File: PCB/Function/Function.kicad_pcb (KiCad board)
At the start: 2 copper layers, 101.6 x 152.4 mm, 47 parts, among them J1 MTA156-3, J2 MTA156-3, J3 MN12, J4 MN12, J5 MN12, J6 MBNF15, J7 MBNF15, U1 AD823, U12 4013, U2 ADR5045, U3 AD823

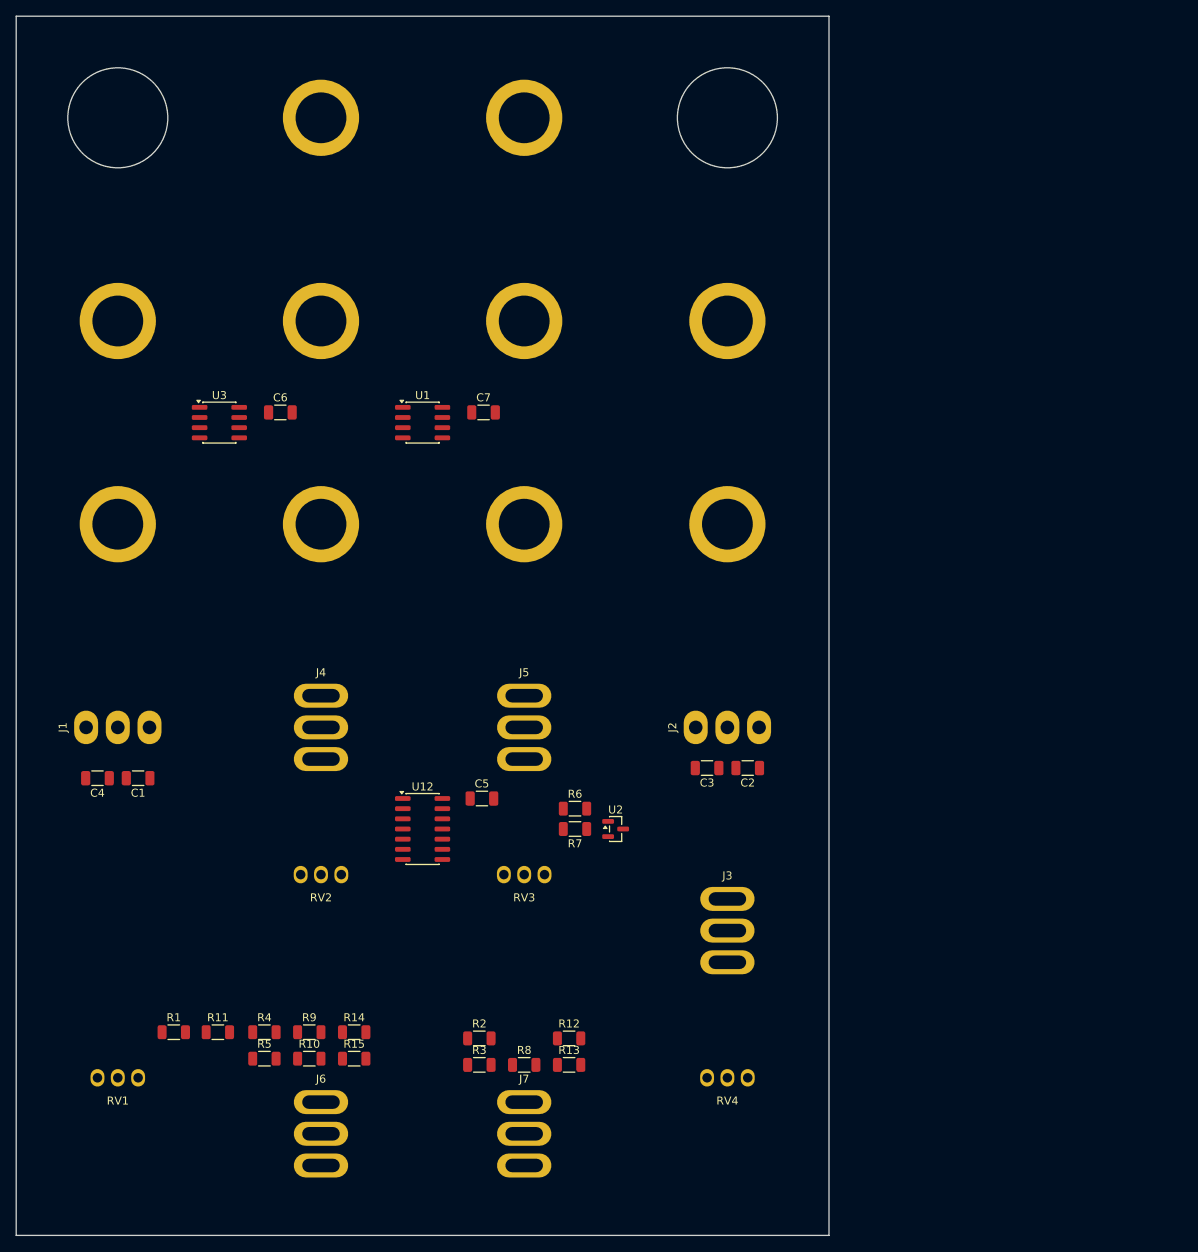
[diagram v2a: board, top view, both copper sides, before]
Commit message: Start placement
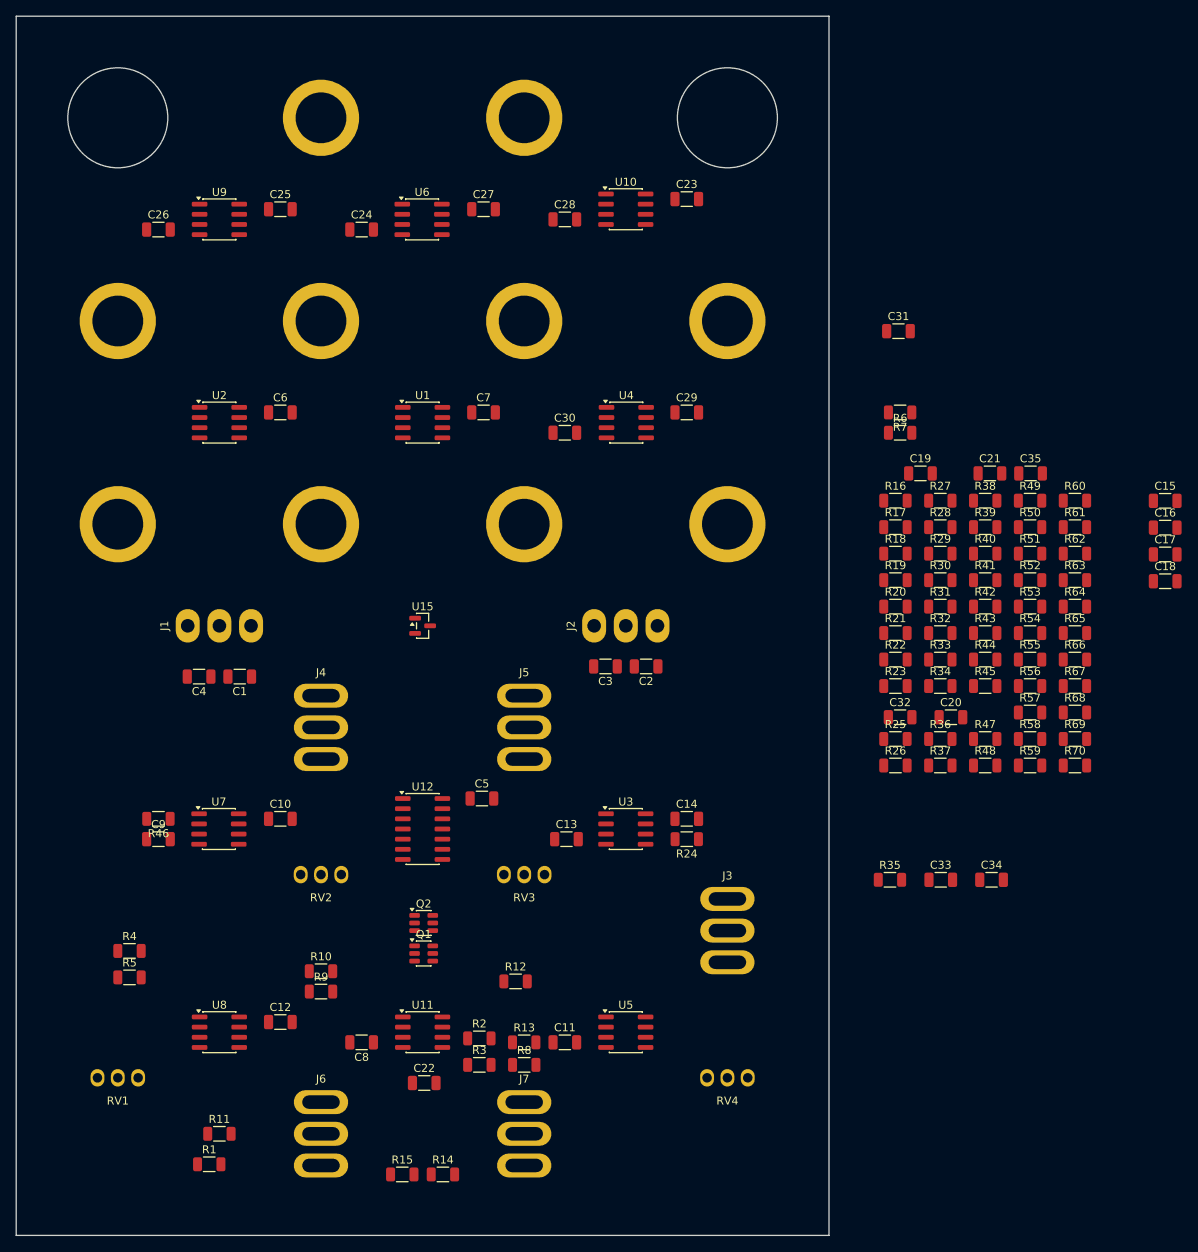
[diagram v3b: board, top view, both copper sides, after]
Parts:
- added C10: 100n, Capacitor_SMD:C_1206_3216Metric, F.Cu at (58.4, 125.7)
- added C11: 100n, Capacitor_SMD:C_1206_3216Metric, F.Cu at (94.0, 153.7)
- added C12: 100n, Capacitor_SMD:C_1206_3216Metric, F.Cu at (58.4, 151.1)
- added C13: 100n, Capacitor_SMD:C_1206_3216Metric, F.Cu at (94.2, 128.3)
- added C14: 100n, Capacitor_SMD:C_1206_3216Metric, F.Cu at (109.2, 125.7)
- added C15: 100n, Capacitor_SMD:C_1206_3216Metric, F.Cu at (169.0, 86.0)
- added C16: 100n, Capacitor_SMD:C_1206_3216Metric, F.Cu at (169.0, 89.3)
- added C17: 100n, Capacitor_SMD:C_1206_3216Metric, F.Cu at (169.0, 92.7)
- added C18: 47p, Capacitor_SMD:C_1206_3216Metric, F.Cu at (169.0, 96.0)
- added C19: 47p, Capacitor_SMD:C_1206_3216Metric, F.Cu at (138.4, 82.5)
- added C20: 47p, Capacitor_SMD:C_1206_3216Metric, F.Cu at (142.2, 113.0)
- added C21: 47p, Capacitor_SMD:C_1206_3216Metric, F.Cu at (147.1, 82.5)
- added C22: 4n7, Capacitor_SMD:C_1206_3216Metric, F.Cu at (76.4, 158.8)
- added C23: 100n, Capacitor_SMD:C_1206_3216Metric, F.Cu at (109.2, 48.3)
- added C24: 100n, Capacitor_SMD:C_1206_3216Metric, F.Cu at (68.6, 52.1)
- added C25: 100n, Capacitor_SMD:C_1206_3216Metric, F.Cu at (58.4, 49.5)
- added C26: 100n, Capacitor_SMD:C_1206_3216Metric, F.Cu at (43.2, 52.1)
- added C27: 100n, Capacitor_SMD:C_1206_3216Metric, F.Cu at (83.8, 49.5)
- added C28: 100n, Capacitor_SMD:C_1206_3216Metric, F.Cu at (94.0, 50.8)
- added C29: 100n, Capacitor_SMD:C_1206_3216Metric, F.Cu at (109.2, 74.9)
- added C30: 100n, Capacitor_SMD:C_1206_3216Metric, F.Cu at (94.0, 77.5)
- added C31: 47p, Capacitor_SMD:C_1206_3216Metric, F.Cu at (135.7, 64.8)
- added C32: 47p, Capacitor_SMD:C_1206_3216Metric, F.Cu at (135.9, 113.0)
- added C33: 47p, Capacitor_SMD:C_1206_3216Metric, F.Cu at (141.0, 133.3)
- added C34: 47p, Capacitor_SMD:C_1206_3216Metric, F.Cu at (147.3, 133.3)
- added C35: 47p, Capacitor_SMD:C_1206_3216Metric, F.Cu at (152.2, 82.5)
- added C8: 100n, Capacitor_SMD:C_1206_3216Metric, F.Cu at (68.6, 153.7)
- added C9: 100n, Capacitor_SMD:C_1206_3216Metric, F.Cu at (43.2, 128.3)
- added Q1: BC847, Package_TO_SOT_SMD:SOT-23-6, F.Cu at (76.3, 142.6)
- added Q2: BCM857, Package_TO_SOT_SMD:SOT-23-6, F.Cu at (76.3, 138.8)
- added R16: 4K7, Resistor_SMD:R_1206_3216Metric, F.Cu at (135.3, 86.0)
- added R17: 150K, Resistor_SMD:R_1206_3216Metric, F.Cu at (135.3, 89.3)
- added R18: 6M8, Resistor_SMD:R_1206_3216Metric, F.Cu at (135.3, 92.6)
- added R19: 47K, Resistor_SMD:R_1206_3216Metric, F.Cu at (135.3, 95.9)
- added R20: 470, Resistor_SMD:R_1206_3216Metric, F.Cu at (135.3, 99.2)
- added R21: 47K, Resistor_SMD:R_1206_3216Metric, F.Cu at (135.3, 102.5)
- added R22: 100K, Resistor_SMD:R_1206_3216Metric, F.Cu at (135.3, 105.8)
- added R23: 33K, Resistor_SMD:R_1206_3216Metric, F.Cu at (135.3, 109.1)
- added R24: 47K, Resistor_SMD:R_1206_3216Metric, F.Cu at (109.2, 128.3)
- added R25: 100K, Resistor_SMD:R_1206_3216Metric, F.Cu at (135.3, 115.8)
- added R26: 33K, Resistor_SMD:R_1206_3216Metric, F.Cu at (135.3, 119.1)
- added R27: 47K, Resistor_SMD:R_1206_3216Metric, F.Cu at (140.9, 86.0)
- added R28: 470, Resistor_SMD:R_1206_3216Metric, F.Cu at (140.9, 89.3)
- added R29: 47K, Resistor_SMD:R_1206_3216Metric, F.Cu at (140.9, 92.6)
- added R30: 47K, Resistor_SMD:R_1206_3216Metric, F.Cu at (140.9, 95.9)
- added R31: 47K, Resistor_SMD:R_1206_3216Metric, F.Cu at (140.9, 99.2)
- added R32: 47K, Resistor_SMD:R_1206_3216Metric, F.Cu at (140.9, 102.5)
- added R33: 470, Resistor_SMD:R_1206_3216Metric, F.Cu at (140.9, 105.8)
- added R34: 47K, Resistor_SMD:R_1206_3216Metric, F.Cu at (140.9, 109.1)
- added R35: 47K, Resistor_SMD:R_1206_3216Metric, F.Cu at (134.6, 133.3)
- added R36: 47K, Resistor_SMD:R_1206_3216Metric, F.Cu at (140.9, 115.8)
- added R37: 47K, Resistor_SMD:R_1206_3216Metric, F.Cu at (140.9, 119.1)
- added R38: 470, Resistor_SMD:R_1206_3216Metric, F.Cu at (146.5, 86.0)
- added R39: 150K, Resistor_SMD:R_1206_3216Metric, F.Cu at (146.5, 89.3)
- added R40: 150K, Resistor_SMD:R_1206_3216Metric, F.Cu at (146.5, 92.6)
- added R41: 33K, Resistor_SMD:R_1206_3216Metric, F.Cu at (146.5, 95.9)
- added R42: 68K, Resistor_SMD:R_1206_3216Metric, F.Cu at (146.5, 99.2)
- added R43: 33K, Resistor_SMD:R_1206_3216Metric, F.Cu at (146.5, 102.5)
- added R44: 68K, Resistor_SMD:R_1206_3216Metric, F.Cu at (146.5, 105.8)
- added R45: 10K, Resistor_SMD:R_1206_3216Metric, F.Cu at (146.5, 109.1)
- added R46: 68K, Resistor_SMD:R_1206_3216Metric, F.Cu at (43.2, 125.7)
- added R47: 4K7, Resistor_SMD:R_1206_3216Metric, F.Cu at (146.5, 115.8)
- added R48: 68K, Resistor_SMD:R_1206_3216Metric, F.Cu at (146.5, 119.1)
- added R49: 4K7, Resistor_SMD:R_1206_3216Metric, F.Cu at (152.1, 86.0)
- added R50: 100K, Resistor_SMD:R_1206_3216Metric, F.Cu at (152.1, 89.3)
- added R51: 100K, Resistor_SMD:R_1206_3216Metric, F.Cu at (152.1, 92.6)
- added R52: 100K, Resistor_SMD:R_1206_3216Metric, F.Cu at (152.1, 95.9)
- added R53: 100K, Resistor_SMD:R_1206_3216Metric, F.Cu at (152.1, 99.2)
- added R54: 100K, Resistor_SMD:R_1206_3216Metric, F.Cu at (152.1, 102.5)
- added R55: 10K, Resistor_SMD:R_1206_3216Metric, F.Cu at (152.1, 105.8)
- added R56: 680K, Resistor_SMD:R_1206_3216Metric, F.Cu at (152.1, 109.1)
- added R57: 100K, Resistor_SMD:R_1206_3216Metric, F.Cu at (152.1, 112.4)
- added R58: 100K, Resistor_SMD:R_1206_3216Metric, F.Cu at (152.1, 115.8)
- added R59: 68K, Resistor_SMD:R_1206_3216Metric, F.Cu at (152.1, 119.1)
- added R60: 100K, Resistor_SMD:R_1206_3216Metric, F.Cu at (157.7, 86.0)
- added R61: 68K, Resistor_SMD:R_1206_3216Metric, F.Cu at (157.7, 89.3)
- added R62: 68K, Resistor_SMD:R_1206_3216Metric, F.Cu at (157.7, 92.6)
- added R63: 100K, Resistor_SMD:R_1206_3216Metric, F.Cu at (157.7, 95.9)
- added R64: 68K, Resistor_SMD:R_1206_3216Metric, F.Cu at (157.7, 99.2)
- added R65: 68K, Resistor_SMD:R_1206_3216Metric, F.Cu at (157.7, 102.5)
- added R66: 100K, Resistor_SMD:R_1206_3216Metric, F.Cu at (157.7, 105.8)
- added R67: 68K, Resistor_SMD:R_1206_3216Metric, F.Cu at (157.7, 109.1)
- added R68: 68K, Resistor_SMD:R_1206_3216Metric, F.Cu at (157.7, 112.4)
- added R69: 100K, Resistor_SMD:R_1206_3216Metric, F.Cu at (157.7, 115.8)
- added R70: 68K, Resistor_SMD:R_1206_3216Metric, F.Cu at (157.7, 119.1)
- added U10: AD823, 5Y:SOIC-8, F.Cu at (101.6, 49.5)
- added U11: ADG419, Package_SO:SOIC-8_3.9x4.9mm_P1.27mm, F.Cu at (76.2, 152.4)
- added U3: AD823, 5Y:SOIC-8, F.Cu at (101.6, 127.0)
- added U4: AD823, 5Y:SOIC-8, F.Cu at (101.7, 76.2)
- added U5: AD823, 5Y:SOIC-8, F.Cu at (101.6, 152.4)
- added U6: AD823, 5Y:SOIC-8, F.Cu at (76.1, 50.8)
- added U7: AD823, 5Y:SOIC-8, F.Cu at (50.7, 127.0)
- added U8: AD823, 5Y:SOIC-8, F.Cu at (50.8, 152.4)
- added U9: AD823, 5Y:SOIC-8, F.Cu at (50.8, 50.8)
- J2: value MTA156-3 -> MTA156-3-PWR
- R10: value 100K -> 68K
- R12: value 470R -> 4K7
- moved R7 66.1 mm to (135.9, 74.9)
- moved R6 62.1 mm to (135.9, 77.5)
- moved U15 35.0 mm to (76.2, 101.6)
- moved R14 21.0 mm to (78.7, 170.2)
- moved R4 19.7 mm to (39.6, 142.2)
- moved R5 19.7 mm to (39.6, 145.6)
- moved C1 18.0 mm to (53.3, 108.0)
- moved J2 18.0 mm to (101.6, 101.6)
- moved C4 18.0 mm to (48.3, 108.0)
- moved J1 18.0 mm to (50.8, 101.6)
- moved C2 18.0 mm to (104.1, 106.7)
- moved C3 18.0 mm to (99.1, 106.7)
- moved R1 17.1 mm to (49.5, 168.9)
- moved R15 15.7 mm to (73.7, 170.2)
- moved R11 12.7 mm to (50.8, 165.1)
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- renumbered U2 to U15, U3 to U2
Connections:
- J**7 pad 1: FREQ_IN -> FREQ
- J4 pad 2: FALL -> FAB
- J5 pad 2: RISE -> RAB
- R10 pad 2: DEK -> GND
- R14 pad 1: FALLP -> FAP
- R15 pad 1: RISEP -> RAP
- U2 pad 5: REF -> Net-(U2B-+)
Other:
- outline, holes or cut-outs redrawn
